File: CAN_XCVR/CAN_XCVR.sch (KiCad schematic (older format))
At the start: 12 parts

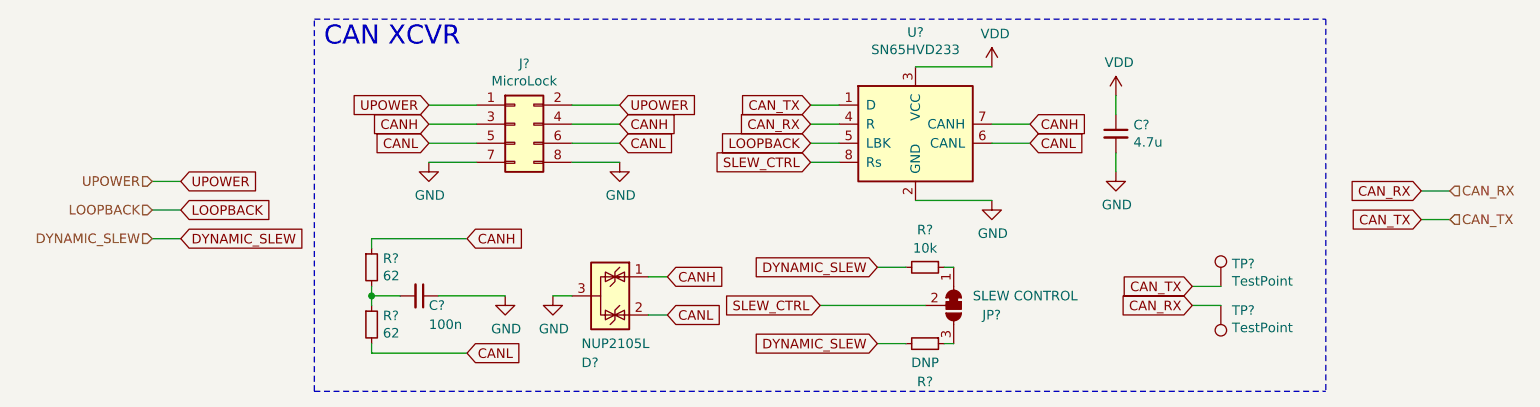
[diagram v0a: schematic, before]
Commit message: update schematic fields, refdes numbers, and cleanup a couple schematics
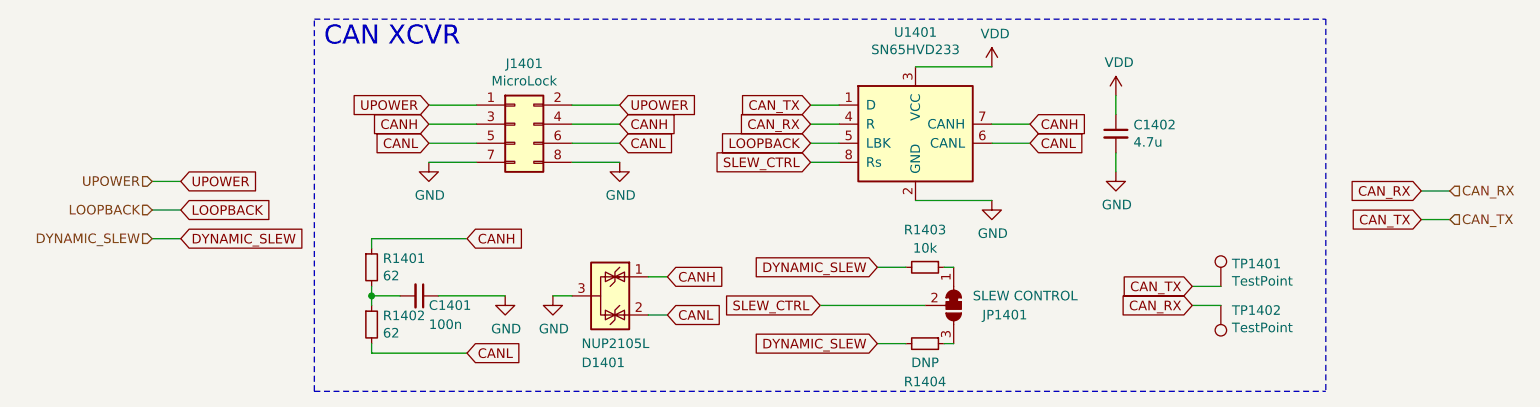
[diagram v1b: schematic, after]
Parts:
- C1401: renamed from C?; DIGIKEY (none) -> 399-1100-1-ND; MANF (none) -> C0603C104Z3VACTU; manf# C0603C104Z3VACTU -> (none)
- C1402: renamed from C?; DIGIKEY (none) -> 311-1820-1-ND; MANF (none) -> CC0603MRX5R6BB475; manf# CC0603MRX5R6BB475 -> (none)
- D1401: renamed from D?; DIGIKEY (none) -> NUP2105LT1GOSCT-ND; MANF (none) -> NUP2105LT1G; manf# NUP2105LT1G -> (none)
- J1401: renamed from J?; DIGIKEY (none) -> WM26819CT-ND; MANF (none) -> 5054480871; manf# 5054480871 -> (none)
- R1401, R1402: renamed from R?; DIGIKEY (none) -> 311-62.0HRCT-ND; MANF (none) -> RC0603FR-0762RL; manf# RC0603FR-0762RL -> (none)
- R1403, R1404: renamed from R?; DIGIKEY (none) -> 311-10KGRCT-ND; MANF (none) -> RC0603JR-0710KL; manf# RC0603JR-0710KL -> (none)
- U1401: renamed from U?; DIGIKEY (none) -> 296-35967-1-ND; MANF (none) -> SN65HVD233DR; manf# SN65HVD233DR -> (none)
- gave numbers to parts that had none: 3
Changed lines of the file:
@@
 $Descr A4 11693 8268
 encoding utf-8
-Sheet 1 6
+Sheet 1 1
 Title ""
 Date ""
@@
 $EndDescr
 $Comp
-L Connector_Generic:Conn_02x04_Odd_Even J?
+L Connector_Generic:Conn_02x04_Odd_Even J1401
 U 1 1 5ED49691
 P 4150 3600
-F 0 "J?" H 4200 3917 50  0000 C CNN
+F 0 "J1401" H 4200 3917 50  0000 C CNN
 F 1 "MicroLock" H 4200 3826 50  0000 C CNN
 F 2 "hardware-sch-blocks:505448-0871" H 4150 3600 50  0001 C CNN
 F 3 "~" H 4150 3600 50  0001 C CNN
-F 4 "5054480871" H 4150 3600 50  0001 C CNN "manf#"
+F 4 "5054480871" H 4150 3600 50  0001 C CNN "MANF"
+F 5 "WM26819CT-ND" H 4150 3600 50  0001 C CNN "DIGIKEY"
 	1    4150 3600
 	1    0    0    -1
 $EndComp
 $Comp
-L power:GND #PWR?
+L power:GND #PWR01404
 U 1 1 5ED49697
 P 4700 3800
-F 0 "#PWR?" H 4700 3550 50  0001 C CNN
+F 0 "#PWR01404" H 4700 3550 50  0001 C CNN
 F 1 "GND" H 4705 3627 50  0000 C CNN
 F 2 "" H 4700 3800 50  0001 C CNN
@@
 $EndComp
 $Comp
-L power:GND #PWR?
+L power:GND #PWR01401
 U 1 1 5ED4969D
 P 3700 3800
-F 0 "#PWR?" H 3700 3550 50  0001 C CNN
+F 0 "#PWR01401" H 3700 3550 50  0001 C CNN
 F 1 "GND" H 3705 3627 50  0000 C CNN
 F 2 "" H 3700 3800 50  0001 C CNN
@@
 	4700 3700 4450 3700
 $Comp
-L Interface_CAN_LIN:SN65HVD233 U?
+L Interface_CAN_LIN:SN65HVD233 U1401
 U 1 1 5ED496B0
 P 6250 3600
-F 0 "U?" H 6250 4081 50  0000 C CNN
+F 0 "U1401" H 6250 4081 50  0000 C CNN
 F 1 "SN65HVD233" H 6250 3990 50  0000 C CNN
 F 2 "Package_SO:SOIC-8_3.9x4.9mm_P1.27mm" H 6250 3100 50  0001 C CNN
 F 3 "http://www.ti.com/lit/ds/symlink/sn65hvd234.pdf" H 6150 4000 50  0001 C CNN
-F 4 "SN65HVD233DR" H 6250 3600 50  0001 C CNN "manf#"
+F 4 "SN65HVD233DR" H 6250 3600 50  0001 C CNN "MANF"
+F 5 "296-35967-1-ND" H 6250 3600 50  0001 C CNN "DIGIKEY"
 	1    6250 3600
 	1    0    0    -1
@@
 	6650 3600 6850 3600
 $Comp
-L power:VDD #PWR?
+L power:VDD #PWR01405
 U 1 1 5ED496BA
 P 6650 3300
-F 0 "#PWR?" H 6650 3150 50  0001 C CNN
+F 0 "#PWR01405" H 6650 3150 50  0001 C CNN
 F 1 "VDD" H 6667 3473 50  0000 C CNN
 F 2 "" H 6650 3300 50  0001 C CNN
@@
 	6650 3300 6250 3300
 $Comp
-L power:GND #PWR?
+L power:GND #PWR01406
 U 1 1 5ED496C1
 P 6650 4000
-F 0 "#PWR?" H 6650 3750 50  0001 C CNN
+F 0 "#PWR01406" H 6650 3750 50  0001 C CNN
 F 1 "GND" H 6655 3827 50  0000 C CNN
 F 2 "" H 6650 4000 50  0001 C CNN
@@
 	6650 4000 6250 4000
 $Comp
-L Device:C_Small C?
+L Device:C_Small C1402
 U 1 1 5ED496C9
 P 7300 3650
-F 0 "C?" H 7392 3696 50  0000 L CNN
+F 0 "C1402" H 7392 3696 50  0000 L CNN
 F 1 "4.7u" H 7392 3605 50  0000 L CNN
 F 2 "Capacitor_SMD:C_0603_1608Metric" H 7300 3650 50  0001 C CNN
 F 3 "~" H 7300 3650 50  0001 C CNN
-F 4 "CC0603MRX5R6BB475" H 7300 3650 50  0001 C CNN "manf#"
+F 4 "CC0603MRX5R6BB475" H 7300 3650 50  0001 C CNN "MANF"
+F 5 "311-1820-1-ND" H 7300 3650 50  0001 C CNN "DIGIKEY"
 	1    7300 3650
 	1    0    0    -1
 $EndComp
 $Comp
-L power:GND #PWR?
+L power:GND #PWR01408
 U 1 1 5ED496CF
 P 7300 3850
-F 0 "#PWR?" H 7300 3600 50  0001 C CNN
+F 0 "#PWR01408" H 7300 3600 50  0001 C CNN
 F 1 "GND" H 7305 3677 50  0000 C CNN
 F 2 "" H 7300 3850 50  0001 C CNN
@@
 $EndComp
 $Comp
-L power:VDD #PWR?
+L power:VDD #PWR01407
 U 1 1 5ED496D5
 P 7300 3450
-F 0 "#PWR?" H 7300 3300 50  0001 C CNN
+F 0 "#PWR01407" H 7300 3300 50  0001 C CNN
 F 1 "VDD" H 7317 3623 50  0000 C CNN
 F 2 "" H 7300 3450 50  0001 C CNN
@@
 	7300 3750 7300 3850
 $Comp
-L Device:R_Small R?
+L Device:R_Small R1402
 U 1 1 5ED496DF
 P 3400 4650
-F 0 "R?" H 3459 4696 50  0000 L CNN
+F 0 "R1402" H 3459 4696 50  0000 L CNN
 F 1 "62" H 3459 4605 50  0000 L CNN
 F 2 "Resistor_SMD:R_0603_1608Metric" H 3400 4650 50  0001 C CNN
 F 3 "~" H 3400 4650 50  0001 C CNN
-F 4 "RC0603FR-0762RL" H 3400 4650 50  0001 C CNN "manf#"
+F 4 "RC0603FR-0762RL" H 3400 4650 50  0001 C CNN "MANF"
 F 5 "" H 3400 4650 50  0001 C CNN "DNP"
+F 6 "311-62.0HRCT-ND" H 3400 4650 50  0001 C CNN "DIGIKEY"
 	1    3400 4650
 	1    0    0    -1
@@
 SLEW_CTRL
 $Comp
-L Device:R_Small R?
+L Device:R_Small R1403
 U 1 1 5ED496EC
 P 6300 4350
-F 0 "R?" V 6104 4350 50  0000 C CNN
+F 0 "R1403" V 6104 4350 50  0000 C CNN
 F 1 "10k" V 6200 4350 50  0000 C CNN
 F 2 "Resistor_SMD:R_0603_1608Metric" H 6300 4350 50  0001 C CNN
 F 3 "~" H 6300 4350 50  0001 C CNN
-F 4 "RC0603JR-0710KL" V 6300 4350 50  0001 C CNN "manf#"
+F 4 "RC0603JR-0710KL" V 6300 4350 50  0001 C CNN "MANF"
+F 5 "311-10KGRCT-ND" H 6300 4350 50  0001 C CNN "DIGIKEY"
 	1    6300 4350
 	0    1    1    0
@@
 LOOPBACK
 $Comp
-L Jumper:SolderJumper_3_Bridged12 JP?
+L Jumper:SolderJumper_3_Bridged12 JP1401
 U 1 1 5ED496F4
 P 6450 4550
-F 0 "JP?" V 6500 4700 50  0000 L CNN
+F 0 "JP1401" V 6500 4700 50  0000 L CNN
 F 1 "SLEW CONTROL" V 6400 4650 50  0000 L CNN
 F 2 "Jumper:SolderJumper-3_P1.3mm_Bridged2Bar12_Pad1.0x1.5mm" H 6450 4550 50  0001 C CNN
@@
 	5750 4550 6300 4550
 $Comp
-L Device:R_Small R?
+L Device:R_Small R1404
 U 1 1 5ED49710
 P 6300 4750
-F 0 "R?" V 6500 4750 50  0000 C CNN
+F 0 "R1404" V 6500 4750 50  0000 C CNN
 F 1 "DNP" V 6400 4750 50  0000 C CNN
 F 2 "Resistor_SMD:R_0603_1608Metric" H 6300 4750 50  0001 C CNN
 F 3 "~" H 6300 4750 50  0001 C CNN
-F 4 "RC0603JR-0710KL" V 6300 4750 50  0001 C CNN "manf#"
+F 4 "RC0603JR-0710KL" V 6300 4750 50  0001 C CNN "MANF"
 F 5 "true" H 6300 4750 50  0001 C CNN "DNP"
+F 6 "311-10KGRCT-ND" H 6300 4750 50  0001 C CNN "DIGIKEY"
 	1    6300 4750
 	0    1    1    0
@@
 	6200 4750 6050 4750
 $Comp
-L Device:R_Small R?
+L Device:R_Small R1401
 U 1 1 5ED4971A
 P 3400 4350
-F 0 "R?" H 3459 4396 50  0000 L CNN
+F 0 "R1401" H 3459 4396 50  0000 L CNN
 F 1 "62" H 3459 4305 50  0000 L CNN
 F 2 "Resistor_SMD:R_0603_1608Metric" H 3400 4350 50  0001 C CNN
 F 3 "~" H 3400 4350 50  0001 C CNN
-F 4 "RC0603FR-0762RL" H 3400 4350 50  0001 C CNN "manf#"
+F 4 "RC0603FR-0762RL" H 3400 4350 50  0001 C CNN "MANF"
 F 5 "" H 3400 4350 50  0001 C CNN "DNP"
+F 6 "311-62.0HRCT-ND" H 3400 4350 50  0001 C CNN "DIGIKEY"
 	1    3400 4350
 	1    0    0    -1
@@
 	3400 4550 3400 4500
 $Comp
-L power:GND #PWR?
+L power:GND #PWR01402
 U 1 1 5ED49721
 P 4100 4500
-F 0 "#PWR?" H 4100 4250 50  0001 C CNN
+F 0 "#PWR01402" H 4100 4250 50  0001 C CNN
 F 1 "GND" H 4105 4327 50  0000 C CNN
 F 2 "" H 4100 4500 50  0001 C CNN
@@
 $EndComp
 $Comp
-L Device:C_Small C?
+L Device:C_Small C1401
 U 1 1 5ED49728
 P 3650 4500
-F 0 "C?" V 3700 4550 50  0000 L CNN
+F 0 "C1401" V 3700 4550 50  0000 L CNN
 F 1 "100n" V 3800 4550 50  0000 L CNN
 F 2 "Capacitor_SMD:C_0603_1608Metric" H 3650 4500 50  0001 C CNN
 F 3 "~" H 3650 4500 50  0001 C CNN
-F 4 "C0603C104Z3VACTU" H 3650 4500 50  0001 C CNN "manf#"
+F 4 "C0603C104Z3VACTU" H 3650 4500 50  0001 C CNN "MANF"
+F 5 "399-1100-1-ND" H 3650 4500 50  0001 C CNN "DIGIKEY"
 	1    3650 4500
 	0    1    1    0
@@
 	3750 4500 4100 4500
 $Comp
-L Power_Protection:NUP2105L D?
+L Power_Protection:NUP2105L D1401
 U 1 1 5ED49733
 P 4650 4500
-F 0 "D?" V 5000 4350 50  0000 L CNN
+F 0 "D1401" V 5000 4350 50  0000 L CNN
 F 1 "NUP2105L" V 4900 4350 50  0000 L CNN
 F 2 "Package_TO_SOT_SMD:SOT-23" H 4875 4450 50  0001 L CNN
 F 3 "http://www.onsemi.com/pub_link/Collateral/NUP2105L-D.PDF" H 4775 4625 50  0001 C CNN
-F 4 "NUP2105LT1G" H 4650 4500 50  0001 C CNN "manf#"
+F 4 "NUP2105LT1G" H 4650 4500 50  0001 C CNN "MANF"
+F 5 "NUP2105LT1GOSCT-ND" H 4650 4500 50  0001 C CNN "DIGIKEY"
 	1    4650 4500
 	0    1    1    0
 $EndComp
 $Comp
-L power:GND #PWR?
+L power:GND #PWR01403
 U 1 1 5ED4973A
 P 4350 4500
-F 0 "#PWR?" H 4350 4250 50  0001 C CNN
+F 0 "#PWR01403" H 4350 4250 50  0001 C CNN
 F 1 "GND" H 4355 4327 50  0000 C CNN
 F 2 "" H 4350 4500 50  0001 C CNN
@@
 CAN_TX
 $Comp
-L Connector:TestPoint TP?
+L Connector:TestPoint TP1401
 U 1 1 5ED49747
 P 7850 4450
-F 0 "TP?" H 7908 4568 50  0000 L CNN
+F 0 "TP1401" H 7908 4568 50  0000 L CNN
 F 1 "TestPoint" H 7908 4477 50  0000 L CNN
 F 2 "TestPoint:TestPoint_Pad_1.0x1.0mm" H 8050 4450 50  0001 C CNN
@@
 $EndComp
 $Comp
-L Connector:TestPoint TP?
+L Connector:TestPoint TP1402
 U 1 1 5ED4974E
 P 7850 4550
-F 0 "TP?" H 7792 4576 50  0000 R CNN
+F 0 "TP1402" H 7792 4576 50  0000 R CNN
 F 1 "TestPoint" H 7792 4667 50  0000 R CNN
 F 2 "TestPoint:TestPoint_Pad_1.0x1.0mm" H 8050 4550 50  0001 C CNN
